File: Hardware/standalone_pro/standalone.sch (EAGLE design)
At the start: 111 parts, among them IC1 STM32F050C6T6A, IC2 AP1212, IC3 IR2104S, IC4 AP1212, Q1 32.768khz, U10 ZXCT1107SA-7, U11 NMOS_2N7002, U12 NMOS_2N7002, U2 FDS6690a, U3 FDS6690a, U4 LM2576S, U5 NMOS_2N7002, U6 NMOS_2N7002, U7 INA213AIDCKT, U8 NMOS_2N7002, X1 KUSBVX, X2 KUSBVX, X3 KUSBVX, X4 KUSBVX

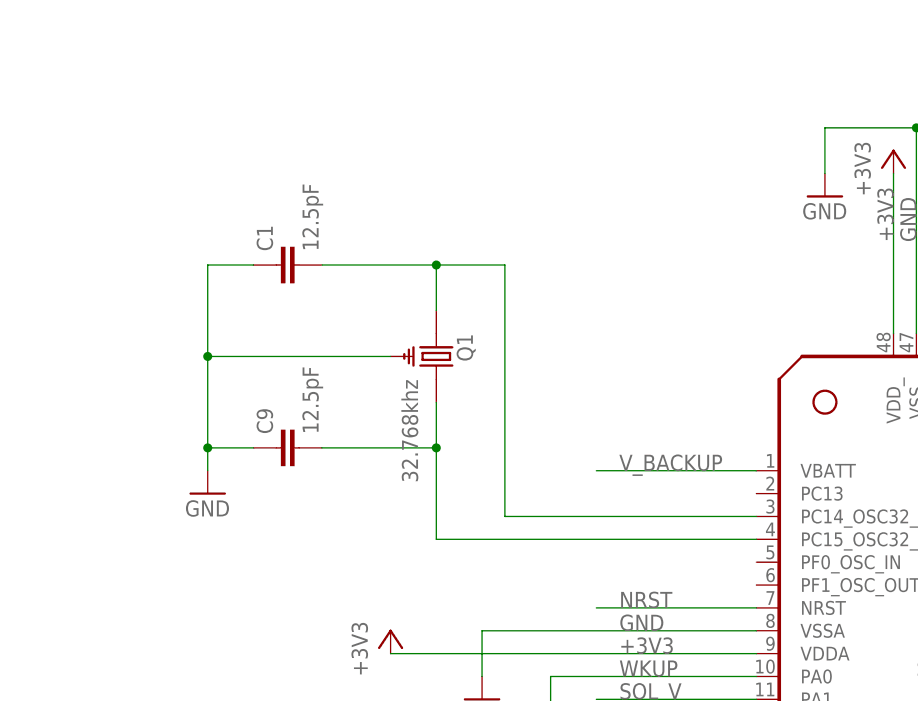
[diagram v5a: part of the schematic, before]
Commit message: Changed RTC XTAL Hardware
Both Home and Pro boards have working XTAL. OC_FARNELL attributes give
correct part numbers.
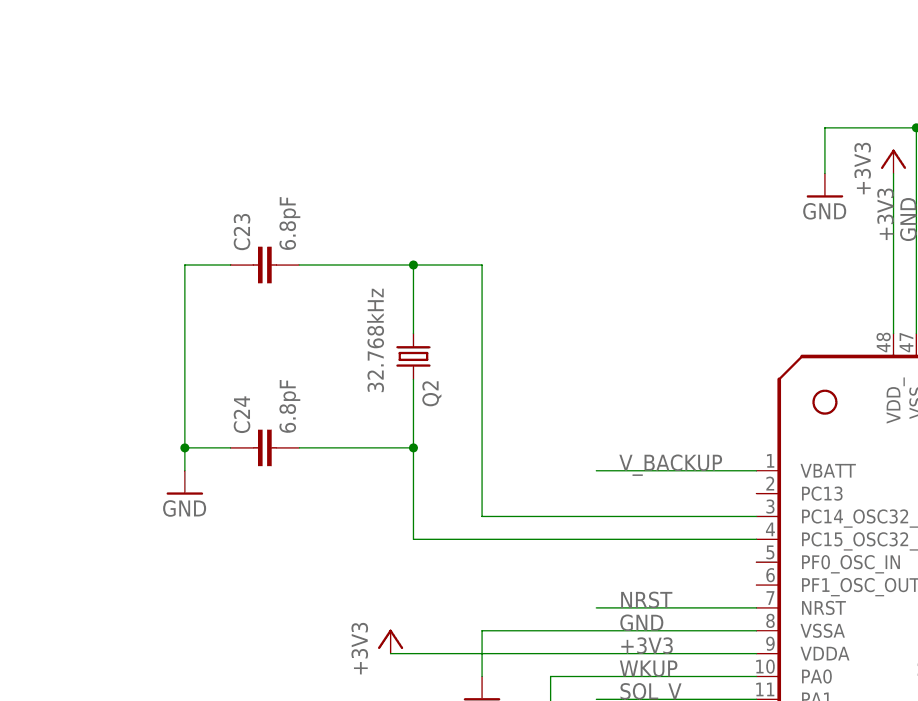
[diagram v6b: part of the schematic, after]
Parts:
- removed C1, C9: 12.5pF, resistor:C-EUC0805K
- removed Q1: 32.768khz, equinox:CRYSTAL_CMJ206T
- added C23, C24: 6.8pF, resistor:C-EUC0603K
- added Q2: 32.768kHz, crystal:MC-306
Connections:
- removed net N$18: C9.2, IC1.PC15_OSC32_OUT, Q1.2
- new net N$49: C24.2, IC1.PC15_OSC32_OUT, Q2.2
- net GND: now also C23.1, C24.1; no longer C1.1, C9.1, Q1.P$1
- net N$1: now also C23.2, Q2.1; no longer C1.2, Q1.1
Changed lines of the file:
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@@
 <?xml version="1.0" encoding="utf-8"?>
 <!DOCTYPE eagle SYSTEM "eagle.dtd">
-<eagle version="6.4">
+<eagle version="6.3">
 <drawing>
 <settings>
@@
 <part name="GND11" library="supply1" deviceset="GND" device="" value="GND"/>
 <part name="GND13" library="supply1" deviceset="GND" device="" value="GND"/>
-<part name="Q1" library="equinox" deviceset="CRYSTAL_CMJ206T" device="" value="32.768khz">
-<attribute name="OC_FARNELL" value="2101358"/>
-</part>
-<part name="C1" library="resistor" deviceset="C-EU" device="C0805K" value="12.5pF"/>
-<part name="C9" library="resistor" deviceset="C-EU" device="C0805K" value="12.5pF"/>
-<part name="GND14" library="supply1" deviceset="GND" device="" value="GND"/>
 <part name="+3V5" library="supply1" deviceset="+3V3" device=""/>
 <part name="GND15" library="supply1" deviceset="GND" device="" value="GND"/>
@@
 </part>
 <part name="U$3" library="equinox" deviceset="CON_MOLEX_39_29_1028" device=""/>
+<part name="C23" library="resistor" deviceset="C-EU" device="C0603K" value="6.8pF">
+<attribute name="OC_FARNELL" value="1856141"/>
+</part>
+<part name="C24" library="resistor" deviceset="C-EU" device="C0603K" value="6.8pF">
+<attribute name="OC_FARNELL" value="1856141"/>
+</part>
+<part name="GND2" library="supply1" deviceset="GND" device="" value="GND"/>
+<part name="Q2" library="crystal" deviceset="MC-306" device="" value="32.768kHz">
+<attribute name="MPN" value="MC-306"/>
+<attribute name="OC_FARNELL" value="1712823"/>
+<attribute name="OC_NEWARK" value="-"/>
+</part>
 </parts>
 <sheets>
@@
 <instance part="GND11" gate="1" x="132.08" y="111.76"/>
 <instance part="GND13" gate="1" x="170.18" y="167.64"/>
-<instance part="Q1" gate="G$1" x="127" y="149.86" rot="R270">
-<attribute name="OC_FARNELL" x="127" y="149.86" size="1.778" layer="96" rot="R270" display="off"/>
-</instance>
-<instance part="C1" gate="G$1" x="109.22" y="160.02" rot="R90"/>
-<instance part="C9" gate="G$1" x="109.22" y="139.7" rot="R90"/>
-<instance part="GND14" gate="1" x="101.6" y="134.62"/>
 <instance part="+3V5" gate="G$1" x="294.64" y="60.96"/>
 <instance part="GND15" gate="1" x="294.64" y="43.18"/>
@@
 <instance part="U$3" gate="CON$1" x="698.5" y="228.6"/>
 <instance part="U$3" gate="CON$2" x="698.5" y="220.98"/>
+<instance part="C23" gate="G$1" x="106.68" y="160.02" rot="R90">
+<attribute name="OC_FARNELL" x="106.68" y="160.02" size="1.778" layer="96" rot="R90" display="off"/>
+</instance>
+<instance part="C24" gate="G$1" x="106.68" y="139.7" rot="R90">
+<attribute name="OC_FARNELL" x="106.68" y="139.7" size="1.778" layer="96" rot="R90" display="off"/>
+</instance>
+<instance part="GND2" gate="1" x="99.06" y="134.62"/>
+<instance part="Q2" gate="P" x="124.46" y="149.86" smashed="yes" rot="R270">
+<attribute name="NAME" x="125.476" y="147.32" size="1.778" layer="95" rot="R270"/>
+<attribute name="VALUE" x="119.38" y="157.48" size="1.778" layer="96" rot="R270"/>
+</instance>
 </instances>
 <busses>
@@
 <segment>
 <pinref part="IC1" gate="1" pin="PC14_OSC32_IN"/>
-<wire x1="162.56" y1="132.08" x2="134.62" y2="132.08" width="0.1524" layer="91"/>
-<wire x1="134.62" y1="132.08" x2="134.62" y2="160.02" width="0.1524" layer="91"/>
-<pinref part="Q1" gate="G$1" pin="1"/>
-<wire x1="127" y1="154.94" x2="127" y2="160.02" width="0.1524" layer="91"/>
-<wire x1="134.62" y1="160.02" x2="127" y2="160.02" width="0.1524" layer="91"/>
-<pinref part="C1" gate="G$1" pin="2"/>
-<wire x1="127" y1="160.02" x2="114.3" y2="160.02" width="0.1524" layer="91"/>
-<junction x="127" y="160.02"/>
-</segment>
-</net>
-<net name="N$18" class="0">
-<segment>
-<pinref part="IC1" gate="1" pin="PC15_OSC32_OUT"/>
-<pinref part="Q1" gate="G$1" pin="2"/>
-<wire x1="162.56" y1="129.54" x2="127" y2="129.54" width="0.1524" layer="91"/>
-<wire x1="127" y1="129.54" x2="127" y2="139.7" width="0.1524" layer="91"/>
-<pinref part="C9" gate="G$1" pin="2"/>
-<wire x1="127" y1="139.7" x2="127" y2="144.78" width="0.1524" layer="91"/>
-<wire x1="114.3" y1="139.7" x2="127" y2="139.7" width="0.1524" layer="91"/>
-<junction x="127" y="139.7"/>
+<wire x1="162.56" y1="132.08" x2="132.08" y2="132.08" width="0.1524" layer="91"/>
+<wire x1="132.08" y1="132.08" x2="132.08" y2="160.02" width="0.1524" layer="91"/>
+<pinref part="C23" gate="G$1" pin="2"/>
+<wire x1="132.08" y1="160.02" x2="124.46" y2="160.02" width="0.1524" layer="91"/>
+<pinref part="Q2" gate="P" pin="1"/>
+<wire x1="124.46" y1="160.02" x2="111.76" y2="160.02" width="0.1524" layer="91"/>
+<wire x1="124.46" y1="152.4" x2="124.46" y2="160.02" width="0.1524" layer="91"/>
+<junction x="124.46" y="160.02"/>
 </segment>
 </net>
@@
 </segment>
 <segment>
-<pinref part="GND14" gate="1" pin="GND"/>
-<wire x1="101.6" y1="137.16" x2="101.6" y2="139.7" width="0.1524" layer="91"/>
-<pinref part="C1" gate="G$1" pin="1"/>
-<wire x1="101.6" y1="139.7" x2="101.6" y2="149.86" width="0.1524" layer="91"/>
-<wire x1="101.6" y1="149.86" x2="101.6" y2="160.02" width="0.1524" layer="91"/>
-<wire x1="101.6" y1="160.02" x2="106.68" y2="160.02" width="0.1524" layer="91"/>
-<pinref part="C9" gate="G$1" pin="1"/>
-<wire x1="106.68" y1="139.7" x2="101.6" y2="139.7" width="0.1524" layer="91"/>
-<junction x="101.6" y="139.7"/>
-<pinref part="Q1" gate="G$1" pin="P$1"/>
-<wire x1="121.92" y1="149.86" x2="101.6" y2="149.86" width="0.1524" layer="91"/>
-<junction x="101.6" y="149.86"/>
-</segment>
-<segment>
 <pinref part="C12" gate="G$1" pin="1"/>
 <pinref part="GND15" gate="1" pin="GND"/>
@@
 <junction x="690.88" y="200.66"/>
 </segment>
+<segment>
+<pinref part="GND2" gate="1" pin="GND"/>
+<wire x1="99.06" y1="137.16" x2="99.06" y2="139.7" width="0.1524" layer="91"/>
+<pinref part="C23" gate="G$1" pin="1"/>
+<wire x1="99.06" y1="139.7" x2="99.06" y2="160.02" width="0.1524" layer="91"/>
+<wire x1="99.06" y1="160.02" x2="104.14" y2="160.02" width="0.1524" layer="91"/>
+<pinref part="C24" gate="G$1" pin="1"/>
+<wire x1="104.14" y1="139.7" x2="99.06" y2="139.7" width="0.1524" layer="91"/>
+<junction x="99.06" y="139.7"/>
+</segment>
 </net>
 <net name="N$39" class="0">
@@
 </segment>
 </net>
+<net name="N$49" class="0">
+<segment>
+<wire x1="162.56" y1="129.54" x2="124.46" y2="129.54" width="0.1524" layer="91"/>
+<wire x1="124.46" y1="129.54" x2="124.46" y2="139.7" width="0.1524" layer="91"/>
+<pinref part="C24" gate="G$1" pin="2"/>
+<wire x1="111.76" y1="139.7" x2="124.46" y2="139.7" width="0.1524" layer="91"/>
+<pinref part="Q2" gate="P" pin="2"/>
+<wire x1="124.46" y1="147.32" x2="124.46" y2="139.7" width="0.1524" layer="91"/>
+<junction x="124.46" y="139.7"/>
+<pinref part="IC1" gate="1" pin="PC15_OSC32_OUT"/>
+</segment>
+</net>

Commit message: Pro Unit Hardware design completed
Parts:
- removed C23, C24: 6.8pF, resistor:C-EUC0603K
- removed U11, U12, U8: NMOS_2N7002, equinox:NMOS_2N7002
- added C1, C9: 1uF, resistor:C-EUC0805K
- added R14: 1.33k, rcl:R-EU_M0805
- added T1: (no value), transistor:BC847B-NPN-SOT23-BEC
- added U1: ZXCT1107SA-7, equinox:ZXCT1107SA-7
- added U9: LM2576S, equinox:LM2576S
- C11, C16, C18, C2: value 1uF -> 100nF
- C12: value 1uF -> 220uF; device resistor:C-EUC0805K -> resistor:CPOL-EUF; OC_FARNELL (none) -> 9695877
- C13, C3: value 100nF -> 10uF
- C14, C5: value 100nF -> 1uF
- C17: value 1uF -> 10uF
- C19: value 1uF -> 100uF; device resistor:C-EUC0805K -> resistor:CPOL-EUE; OC_FARNELL (none) -> 1539489
- C20: value 10uF -> 1uF
- C21, C4: value 100uF -> 1uF; device resistor:CPOL-EUE -> resistor:C-EUC0805K; OC_FARNELL 1539489 -> (none)
- C6: value 220uF -> 6.8pF; device resistor:CPOL-EUF -> resistor:C-EUC0603K; OC_FARNELL 9695877 -> 1856141
- C7: value 10uF -> 6.8pF; device resistor:C-EUC0805K -> resistor:C-EUC0603K; OC_FARNELL (none) -> 1856141
- C8: value 10uF -> 100uF; device resistor:C-EUC0805K -> resistor:CPOL-EUE; OC_FARNELL (none) -> 1539489
- CONTR: device resistor:R-TRIMM3304W -> equinox:R_TRIMM_TC33X
- D1: value SSB43L -> BZX384-C3V6; device equinox:DIODE_SSB43L -> equinox:BZX384-C3V6; OC_FARNELL 1336556 -> (none)
- D3: value SSB43L -> US1D; device equinox:DIODE_SSB43L -> diode:DIODE-DO-214AC; OC_FARNELL 1336556 -> 1625280
- D4: value US1D -> SSB43L; device diode:DIODE-DO-214AC -> equinox:DIODE_SSB43L; OC_FARNELL 1625280 -> 1336556
- D5: value BZX384-C3V6 -> SSB43L; device equinox:BZX384-C3V6 -> equinox:DIODE_SSB43L; OC_FARNELL (none) -> 1336556
- IC1: value STM32F050C6T6A -> IR2104S; device equinox:STM32F050C6T6A -> equinox:IR2104S; OC_FARNELL 2115059 -> 8638756
- IC2: value AP1212 -> STM32F050C6T6A; device equinox:AP1212 -> equinox:STM32F050C6T6A; OC_FARNELL 1825302 -> 2115059
- IC3: value IR2104S -> AP1212; device equinox:IR2104S -> equinox:AP1212; OC_FARNELL 8638756 -> 1825302
- L_MPPT: device equinox:INDUC_BOURNES_SDR1806 -> equinox:INDUC_MURATA_1433428C
- R1: value 75k -> 1k65; device resistor:R-EU_M0805 -> rcl:R-EU_M0805
- R10: value 5 -> 1k; device rcl:R-EU_M0805 -> resistor:R-EU_M0805
- R11: value 75k -> 200; device resistor:R-EU_M0805 -> rcl:R-EU_M0805
- R12: value 49.9k -> 100
- R13, R16: value 75k -> 10K; device resistor:R-EU_M0805 -> rcl:R-EU_M0805
- R15: value 49.9k -> 10K; device resistor:R-EU_M0805 -> rcl:R-EU_M0805
- R17: value 49.9k -> 10; device resistor:R-EU_M0805 -> rcl:R-EU_M0805
- R18: value 75k -> 10; device resistor:R-EU_M0805 -> rcl:R-EU_M0805
- R19: value 49.9k -> 0R
- R2: value 200 -> 1k; device rcl:R-EU_M0805 -> resistor:R-EU_M0805
- R20: device rcl:R-EU_M0805 -> resistor:R-EU_M0805
- R22: value 0R -> 1k; device resistor:R-EU_M0805 -> rcl:R-EU_M0805
- R23, R29: value 1k -> 75k
- R24: value 1k -> 49.9k
- R25: value 10K -> 75k; device rcl:R-EU_M0805 -> resistor:R-EU_M0805
- R26: value 10K -> 49.9k; device rcl:R-EU_M0805 -> resistor:R-EU_M0805
- R27: value 10 -> 75k; device rcl:R-EU_M0805 -> resistor:R-EU_M0805
- R28: value 10 -> 49.9k; device rcl:R-EU_M0805 -> resistor:R-EU_M0805
- R3: value 10K -> 10M; device rcl:R-EU_M0805 -> resistor:R-EU_M0805
- R30: value 1k65 -> 49.9k; device rcl:R-EU_M0805 -> resistor:R-EU_M0805
- R31: value 10M -> 75k
- R4: value 1.33k -> 10K
- R5: value 10K -> 1.33k
- R6: value 1.33k -> 200
- R8: value 200 -> 5
- U10: value ZXCT1107SA-7 -> NMOS_2N7002; device equinox:ZXCT1107SA-7 -> equinox:NMOS_2N7002
- U2, U3: value FDS6690a -> NMOS_2N7002; device equinox:DMS3016SSS-13 -> equinox:NMOS_2N7002; MPN (none) -> 2N7002-7-F; OC_FARNELL 9845275 -> 1713823; OC_NEWARK (none) -> 25R5679; PACKAGE (none) -> SOT-23-3; SUPPLIER (none) -> DIODES INC.
- U4: value LM2576S -> FDS6690a; device equinox:LM2576S -> equinox:DMS3016SSS-13; OC_FARNELL 1469178 -> 9845275
- U5: value NMOS_2N7002 -> FDS6690a; device equinox:NMOS_2N7002 -> equinox:DMS3016SSS-13; OC_FARNELL (none) -> 9845275
- renumbered Q2 to Q1
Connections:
- net +3V3: now also C16.2, C21.2, IC2.VDD, IC2.VDDA, IC2.VDD_, R15.2; no longer C12.2, C13.2, IC1.VDD, IC1.VDDA, IC1.VDD_, R25.2
- net +5V: now also C20.2, IC3.IN, R19.2, U9.FB; no longer C17.2, IC2.IN, R22.2, U4.FB
- net 12V_OUT_EN: now also IC2.PA12, R22.1; no longer IC1.PA12, R20.1
- net BATT_I: now also IC2.PA4; no longer IC1.PA4
- net BATT_V: now also C13.2, IC2.PA3, R13.1, R14.2; no longer C8.2, IC1.PA3, R5.1, R6.2
- net CC_EN: now also IC2.PB0, R6.1; no longer IC1.PB0, R8.1
- net CC_PWM: now also IC2.PA7; no longer IC1.PA7
- net GND: now also C1.1, C12.-, C19.-, C2.1, C20.1, C21.1, C4.1, C5.2, C6.1, C8.-, C9.1, D1.A, D3.A, D5.ANODE, IC1.COM, IC2.BOOT0, IC2.VSS, IC2.VSSA, IC2.VSS_, IC3.GND, R1.1, R14.1, R16.1, R2.2, R24.1, R28.1, R5.1, T1.E, U10.S, U5.S_2, U5.S_3, U9.GND, U9.GND_2, U9.~ON~/OFF; no longer C10.2, C11.1, C12.1, C17.1, C19.1, C21.-, C23.1, C24.1, C4.-, C6.-, C8.1, D1.ANODE, D4.A, D5.A, IC1.BOOT0, IC1.VSS, IC1.VSSA, IC1.VSS_, IC2.GND, IC3.COM, R12.1, R15.1, R17.1, R19.1, R24.2, R4.1, R6.1, U11.S, U3.S_2, U3.S_3, U4.GND, U4.GND_2, U4.~ON~/OFF, U8.S
- net LCD_BK_EN: now also IC2.PB1, R20.1; no longer IC1.PB1, R23.1
- net LCD_D4: now also IC2.PB15; no longer IC1.PB15
- net LCD_D5: now also IC2.PB14; no longer IC1.PB14
- net LCD_D6: now also IC2.PB13; no longer IC1.PB13
- net LCD_D7: now also IC2.PB12; no longer IC1.PB12
- net LCD_E: now also IC2.PB11; no longer IC1.PB11
- net LCD_RS: now also IC2.PB2; no longer IC1.PB2
- net LCD_RW: now also IC2.PB10; no longer IC1.PB10
- net N$1: now also C6.2, IC2.PC14_OSC32_IN; no longer C23.2, IC1.PC14_OSC32_IN
- net N$10: now also C10.1, IC1.VB; no longer C2.1, IC3.VB
- net N$11: now also R9.1, U5.G; no longer R10.1, U3.G
- net N$12: now also C12.+, D4.ANODE, R11.1; no longer C6.+, D3.ANODE, R2.1
- net N$13: now also IC1.LO, R9.2; no longer IC3.LO, R10.2
- net N$14: now also R8.1, U4.G; no longer R9.1, U2.G
- net N$15: now also C11.2, R11.2; no longer C5.2, R2.2
- net N$16: now also C5.1, C8.+, C9.2, IC1.VCC, R4.2, U1.S-, U4.D, U4.D_2, U4.D_3, U4.D_4; no longer C10.1, C11.2, C4.+, IC3.VCC, R3.2, U10.S-, U2.D, U2.D_2, U2.D_3, U2.D_4
- net N$17: now also R35.1, R36.2; no longer R33.1, R34.2
- net N$19: now also R19.1; no longer R22.1
- net N$20: now also R25.1, R26.2; no longer R16.1, R17.2
- net N$21: now also U9.OUT; no longer U4.OUT
- net N$22: now also IC2.PA8, R10.1; no longer IC1.PA8, R29.1
- net N$23: now also IC2.PB9; no longer IC1.PB9
- net N$24: now also IC2.PB8; no longer IC1.PB8
- net N$26: now also IC2.PB7; no longer IC1.PB7
- net N$27: now also IC2.PB6; no longer IC1.PB6
- net N$28: now also IC2.PB5; no longer IC1.PB5
- net N$29: now also IC2.PB4; no longer IC1.PB4
- net N$3: now also IC1.SD/, R6.2; no longer IC3.SD/, R8.2
- net N$30: now also IC2.PA15; no longer IC1.PA15
- net N$31: now also T1.C; no longer U6.D
- net N$32: now also R20.2, T1.B; no longer R23.2, U6.G
- net N$33: now also R23.1, R24.2; no longer R11.1, R12.2
- net N$34: now also R27.1, R28.2; no longer R13.1, R15.2
- net N$35: now also R22.2, U10.G; no longer R20.2, U5.G
- net N$36: now also R29.1, R30.2; no longer R18.1, R19.2
- net N$38: now also U1.S+; no longer U10.S+
- net N$39: now also R15.1, R16.2; no longer R25.1, R26.2
- net N$4: now also D5.CATHODE, R18.2; no longer D1.CATHODE, R28.2
- net N$40: now also C17.2, R17.1; no longer C20.2, R27.1
- net N$41: now also C17.1, R18.1; no longer C20.1, R28.1
- net N$42: now also R12.2, U6.D; no longer U8.D
- net N$43: now also R10.2, U6.G; no longer R29.2, U8.G
- net N$44: now also C4.2, R3.2, U3.G; no longer C16.2, R31.2, U11.G
- net N$45: now also U2.S, U3.D; no longer U11.D, U12.S
- net N$47: now also R33.1, R34.2; no longer R35.1, R36.2
- net N$49: now also C7.2, IC2.PC15_OSC32_OUT; no longer C24.2, IC1.PC15_OSC32_OUT
- net N$5: now also R31.1; no longer R1.1
- net N$50: now also U10.D; no longer U5.D
- net N$6: now also C10.2, C11.1, D3.C, IC1.VS, U4.S, U4.S_2, U4.S_3, U5.D, U5.D_2, U5.D_3, U5.D_4; no longer C2.2, C5.1, D4.C, IC3.VS, U2.S, U2.S_2, U2.S_3, U3.D, U3.D_2, U3.D_3, U3.D_4
- net N$7: now also IC1.HO, R8.2; no longer IC3.HO, R9.2
- net N$8: now also IC1.IN; no longer IC3.IN
- net NRST: now also IC2.NRST, U2.D; no longer IC1.NRST, U12.D
- net SOL_I: now also C1.2, D1.C, IC2.PA2, R1.2, U1.OUT; no longer C19.2, D5.C, IC1.PA2, R30.2, U10.OUT
- net SOL_V: now also C3.2, IC2.PA1, R4.1, R5.2; no longer C7.2, IC1.PA1, R3.1, R4.2
- net SWCLK: now also IC2.PA14; no longer IC1.PA14
- net SWDIO: now also IC2.PA13; no longer IC1.PA13
- net SWO: now also IC2.PB3; no longer IC1.PB3
- net USART1_RX: now also IC2.PA10; no longer IC1.PA10
- net USART1_TX: now also IC2.PA9; no longer IC1.PA9
- net USB_EN1: now also IC2.PF7, IC3.EN1; no longer IC1.PF7, IC2.EN1
- net USB_EN2: now also IC2.PF6, IC3.EN2; no longer IC1.PF6, IC2.EN2
- net USB_FLG1: now also IC2.PA5, IC3.FLG1; no longer IC1.PA5, IC2.FLG1
- net USB_FLG2: now also IC2.PA6, IC3.FLG2; no longer IC1.PA6, IC2.FLG2
- net USB_OUT1: now also IC3.OUT1, R23.2, R27.2, R31.2, R35.2; no longer IC2.OUT1, R1.2, R11.2, R13.2, R33.2
- net USB_OUT2: now also IC3.OUT2, R25.2, R29.2, R33.2; no longer IC2.OUT2, R16.2, R18.2, R35.2
- net V_BACKUP: now also IC2.VBATT; no longer IC1.VBATT
- net V_LOAD: now also C19.+, D4.CATHODE, R12.1, R13.2, R17.2, U9.VIN; no longer C21.+, D3.CATHODE, R27.2, R5.2, U4.VIN
- net WKUP: now also C2.2, IC2.PA0, R2.1, R3.1, U2.G; no longer C3.2, IC1.PA0, R24.1, R31.1, U12.G
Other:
- note removed: "TODO: - Contrast Adjust Pot needs changing - Swap MOS with BJT"
- moved on the sheet: C10, C11, C13, C14, C15, C16, C17, C18, C2, C20, C3, C5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

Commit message: Small Changes to Pro Board and Gerbers Made
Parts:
- renumbered U$3 to INVERTER
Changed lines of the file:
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@@
 <attribute name="OC_FARNELL" value="1625280"/>
 </part>
-<part name="U$3" library="equinox" deviceset="CON_MOLEX_39_29_1028" device=""/>
+<part name="INVERTER" library="equinox" deviceset="CON_MOLEX_39_29_1028" device=""/>
 <part name="C6" library="resistor" deviceset="C-EU" device="C0603K" value="6.8pF">
 <attribute name="OC_FARNELL" value="1856141"/>
@@
 <attribute name="OC_FARNELL" x="655.32" y="177.8" size="1.778" layer="96" rot="R180" display="off"/>
 </instance>
-<instance part="U$3" gate="CON$1" x="698.5" y="228.6"/>
-<instance part="U$3" gate="CON$2" x="698.5" y="220.98"/>
+<instance part="INVERTER" gate="CON$1" x="698.5" y="228.6"/>
+<instance part="INVERTER" gate="CON$2" x="698.5" y="220.98"/>
 <instance part="C6" gate="G$1" x="106.68" y="160.02" rot="R90">
 <attribute name="OC_FARNELL" x="106.68" y="160.02" size="1.778" layer="96" rot="R90" display="off"/>
@@
 <junction x="665.48" y="205.74"/>
 <wire x1="688.34" y1="203.2" x2="688.34" y2="228.6" width="0.1524" layer="91"/>
-<pinref part="U$3" gate="CON$1" pin="S"/>
+<pinref part="INVERTER" gate="CON$1" pin="S"/>
 <wire x1="688.34" y1="228.6" x2="695.96" y2="228.6" width="0.1524" layer="91"/>
 <pinref part="DC4" gate="G$1" pin="PAD1"/>
@@
 <wire x1="693.42" y1="167.64" x2="690.88" y2="167.64" width="0.1524" layer="91"/>
 <junction x="690.88" y="167.64"/>
-<pinref part="U$3" gate="CON$2" pin="S"/>
+<pinref part="INVERTER" gate="CON$2" pin="S"/>
 <wire x1="695.96" y1="220.98" x2="690.88" y2="220.98" width="0.1524" layer="91"/>
 <wire x1="690.88" y1="220.98" x2="690.88" y2="200.66" width="0.1524" layer="91"/>
